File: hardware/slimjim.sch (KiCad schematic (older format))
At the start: 9 parts, among them J1 USB, P1 CONN_01X12, P2 CONN_01X12, P3 CONN_01X12, P4 CONN_01X12, P5 CONN_01X12, P6 CONN_01X12, SW1 SW_PUSH

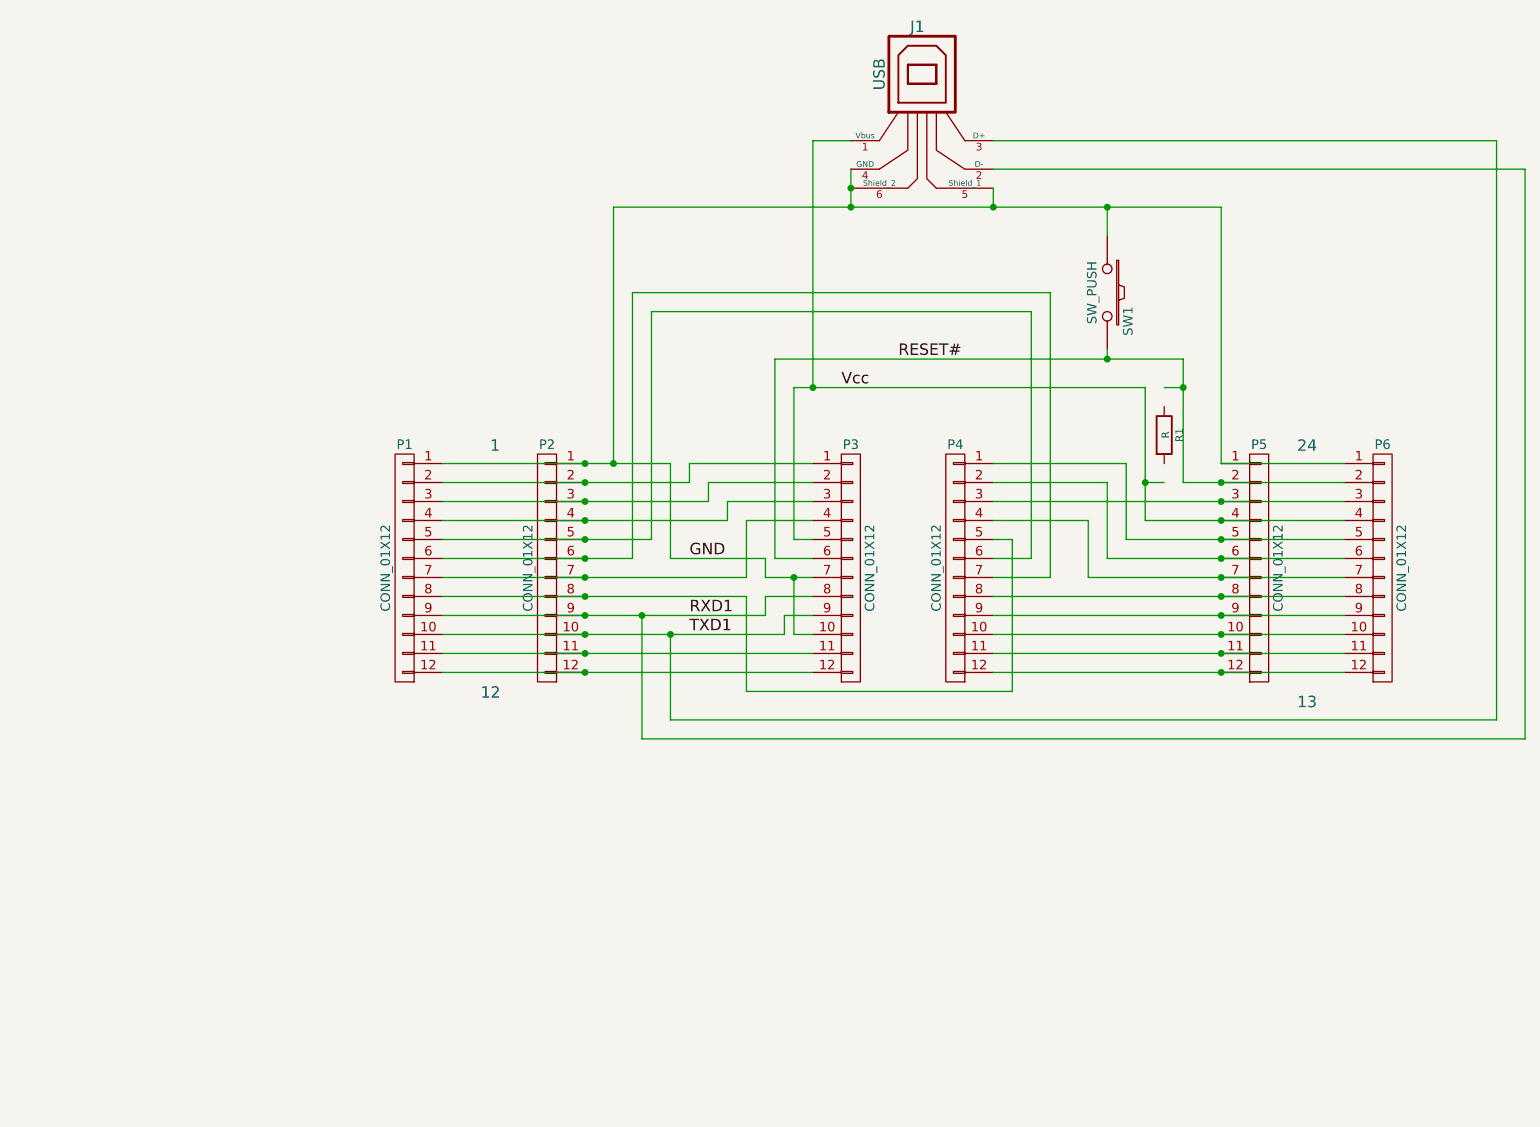
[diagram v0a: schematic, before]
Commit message: Replace generic pin headers with actual parts.
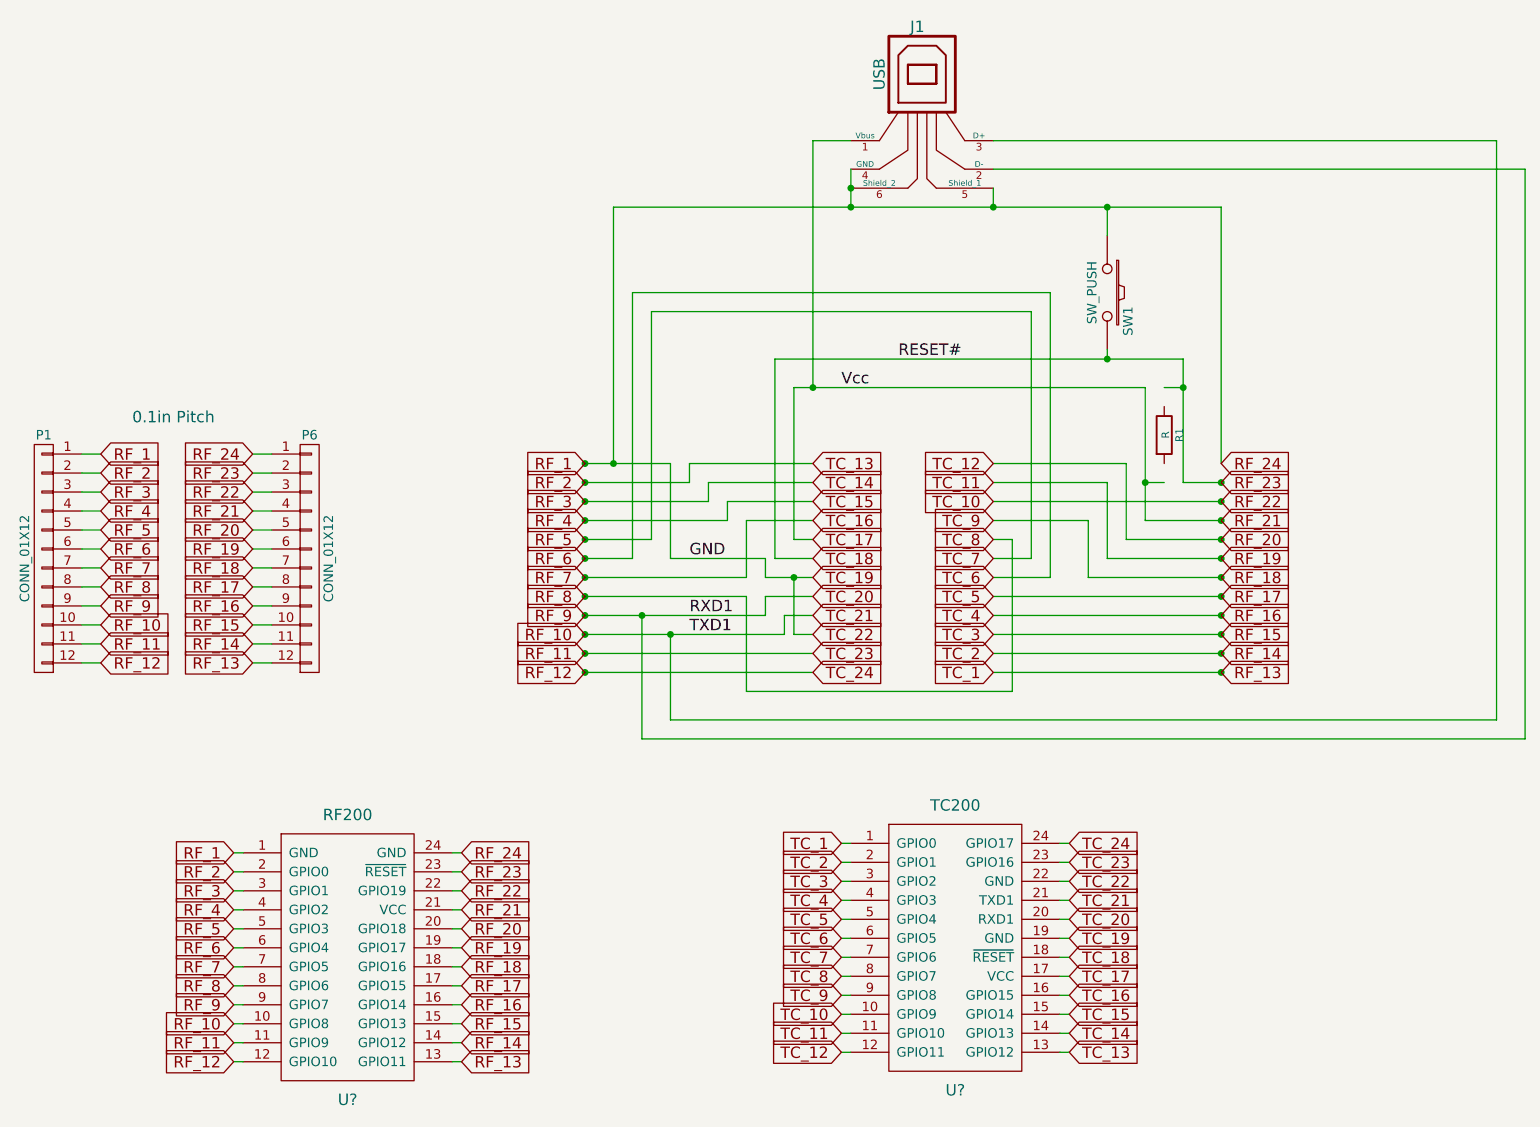
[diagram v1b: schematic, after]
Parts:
- removed P2, P3, P4, P5: CONN_01X12, symbol CONN_01X12
- added U?: RF200, symbol RF200
- added U?: TC200, symbol TC200
- SW1: footprint (none) -> _CrumpPrints:6x6mm_pushbutton
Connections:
- net RF_2: now reaches P1.2 (P2)
- net RF_2: now also U?.13 (GPIO12), U?.2 (GPIO0)
- net RF_11: now reaches P1.11 (P11)
- net RF_11: now also U?.11 (GPIO9), U?.23 (GPIO16)
- net RF_12: now reaches P1.12 (P12)
- net RF_12: now also U?.12 (GPIO10), U?.24 (GPIO17)
- net RF_3: now reaches P1.3 (P3)
- net RF_3: now also U?.14 (GPIO13), U?.3 (GPIO1)
- net RF_4: now reaches P1.4 (P4)
- net RF_4: now also U?.15 (GPIO14), U?.4 (GPIO2)
- net RF_7: now reaches P1.7 (P7)
- net RF_7: now also U?.16 (GPIO15), U?.7 (GPIO5)
- net RF_20: now reaches P6.5 (P5)
- net RF_20: now also U?.12 (GPIO11), U?.20 (GPIO18)
- net RF_15: now reaches P6.10 (P10)
- net RF_15: now also U?.15 (GPIO13), U?.3 (GPIO2)
- net RF_14: now reaches P6.11 (P11)
- net RF_14: now also U?.14 (GPIO12), U?.2 (GPIO1)
- net RF_13: now reaches P6.12 (P12)
- net RF_13: now also U?.1 (GPIO0), U?.13 (GPIO11)
- net RF_19: now reaches P6.6 (P6)
- net RF_19: now also U?.11 (GPIO10), U?.19 (GPIO17)
- net RF_22: now reaches P6.3 (P3)
- net RF_22: now also U?.10 (GPIO9), U?.22 (GPIO19)
- net RF_18: now reaches P6.7 (P7)
- net RF_18: now also U?.18 (GPIO16), U?.9 (GPIO8)
- net RF_8: now reaches P1.8 (P8)
- net RF_8: now also U?.8 (GPIO6), U?.8 (GPIO7)
- net RF_5: now reaches P1.5 (P5)
- net RF_5: now also U?.5 (GPIO3), U?.7 (GPIO6)
- net RF_6: now reaches P1.6 (P6)
- net RF_6: now also U?.6 (GPIO4), U?.6 (GPIO5)
- net RF_17: now reaches P6.8 (P8)
- net RF_17: now also U?.17 (GPIO15), U?.5 (GPIO4)
- net RF_16: now reaches P6.9 (P9)
- net RF_16: now also U?.16 (GPIO14), U?.4 (GPIO3)
- net GND renamed RF_1
- net RF_1: now also U?.1 (GND), U?.19 (GND), U?.22 (GND), U?.24 (GND)
- net RESET# renamed RF_23
- net RF_23: now also U?.18 (~RESET), U?.23 (~RESET)
- net RXD1 renamed RF_9
- net RF_9: now also U?.20 (RXD1), U?.9 (GPIO7)
- net TXD1 renamed RF_10
- net RF_10: now also U?.10 (GPIO8), U?.21 (TXD1)
- net Vcc renamed RF_21
- net RF_21: now also U?.17 (VCC), U?.21 (VCC)
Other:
- note added: "0.1in Pitch"
- note removed: "1"
- note removed: "12"
- note removed: "13"
- note removed: "24"
- moved on the sheet: P1, P6

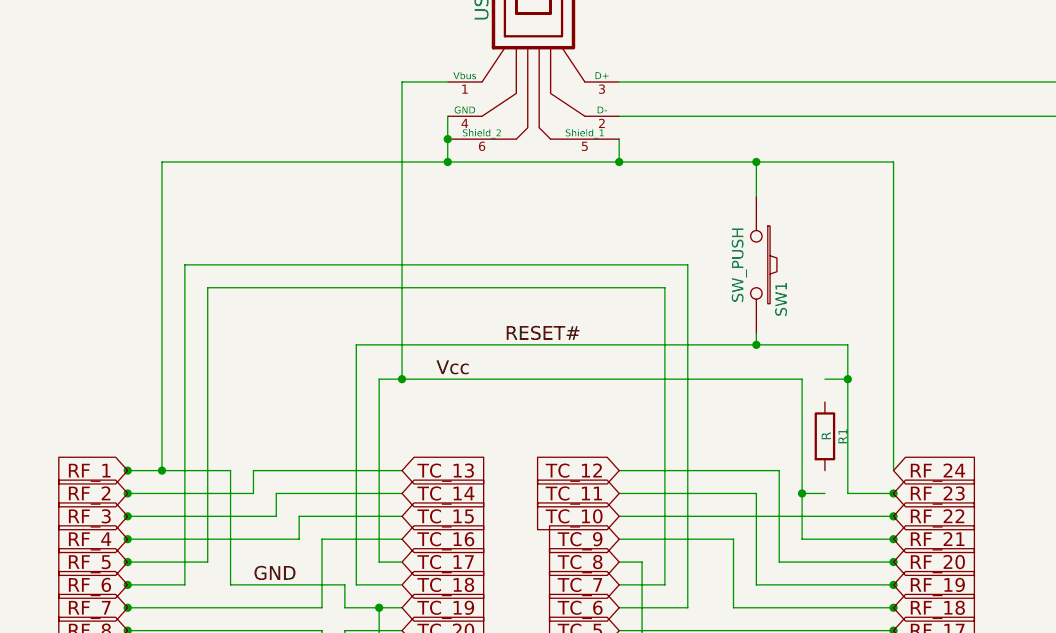
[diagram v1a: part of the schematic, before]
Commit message: Make tiny tweak to a wire in schematic.
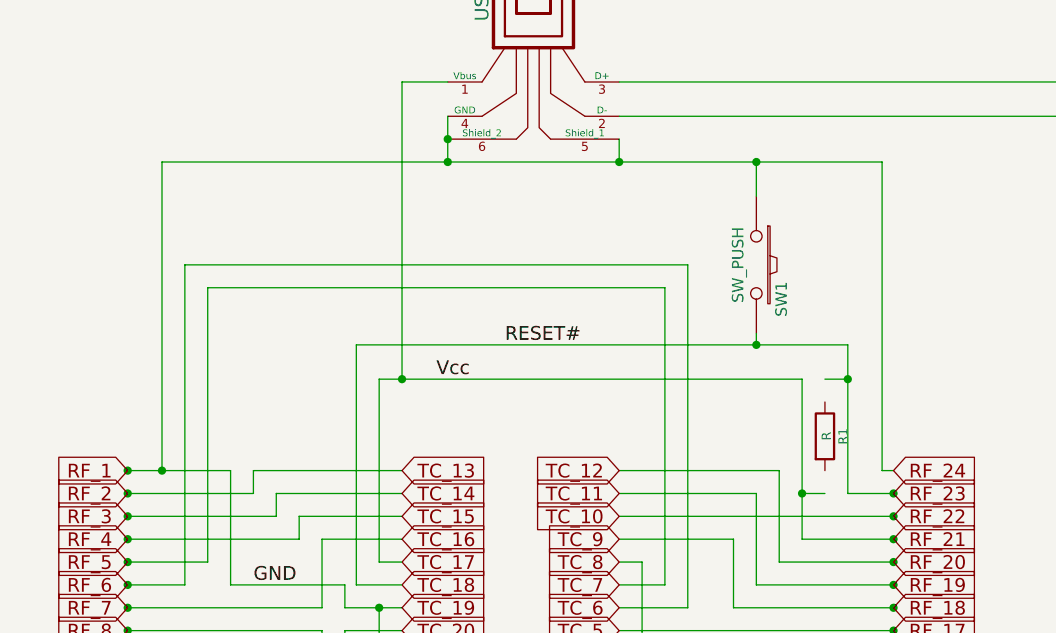
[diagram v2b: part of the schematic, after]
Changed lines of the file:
@@
 	6550 1900 6550 1800
 Wire Wire Line
-	4550 1900 7750 1900
+	4550 1900 7700 1900
 Connection ~ 5800 1800
 Wire Wire Line
@@
 Connection ~ 4400 4350
 Wire Wire Line
-	7750 1900 7750 3250
+	7700 1900 7700 3250
 Connection ~ 6550 1900
 Connection ~ 7750 3350
@@
 Wire Wire Line
 	6950 5250 6900 5250
+Wire Wire Line
+	7700 3250 7750 3250
 $EndSCHEMATC

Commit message: Initial part placement.
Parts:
- J1: footprint (none) -> Connect:USB_A
- P1: footprint (none) -> _CrumpPrints:Header_1x12_100
- P2: renamed from P6; footprint (none) -> _CrumpPrints:Header_1x12_100
- R1: footprint (none) -> Resistors_SMD:R_0805_HandSoldering
- U1: renamed from U?; footprint (none) -> _CrumpPrints:RF200
- U2: renamed from U?; footprint (none) -> _CrumpPrints:TC200
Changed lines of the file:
@@
 F 0 "J1" H 6150 1750 60  0000 C CNN
 F 1 "USB" V 5950 1500 60  0000 C CNN
-F 2 "" H 6200 1350 60  0001 C CNN
+F 2 "Connect:USB_A" H 6200 1350 60  0001 C CNN
 F 3 "" H 6200 1350 60  0000 C CNN
 	1    6200 1350
@@
 Connection ~ 4850 4150
 $Comp
-L CONN_01X12 P6
+L CONN_01X12 P2
 U 1 1 56F37C15
 P 2950 3750
-F 0 "P6" H 2950 4400 50  0000 C CNN
+F 0 "P2" H 2950 4400 50  0000 C CNN
 F 1 "CONN_01X12" V 3050 3750 50  0000 C CNN
-F 2 "" H 2950 3750 60  0001 C CNN
+F 2 "_CrumpPrints:Header_1x12_100" H 2950 3750 60  0001 C CNN
 F 3 "" H 2950 3750 60  0000 C CNN
 	1    2950 3750
@@
 F 0 "P1" H 1550 4400 50  0000 C CNN
 F 1 "CONN_01X12" V 1650 3750 50  0000 C CNN
-F 2 "" H 1550 3750 60  0001 C CNN
+F 2 "_CrumpPrints:Header_1x12_100" H 1550 3750 60  0001 C CNN
 F 3 "" H 1550 3750 60  0000 C CNN
 	1    1550 3750
@@
 F 0 "R1" V 7530 3100 40  0000 C CNN
 F 1 "R" V 7457 3101 40  0000 C CNN
-F 2 "" V 7380 3100 30  0001 C CNN
+F 2 "Resistors_SMD:R_0805_HandSoldering" V 7380 3100 30  0001 C CNN
 F 3 "" H 7450 3100 30  0000 C CNN
 	1    7450 3100
@@
 0.1in Pitch
 $Comp
-L RF200 U?
+L RF200 U1
 U 1 1 56FE09B4
 P 3150 5850
-F 0 "U?" H 3150 5100 60  0000 C CNN
+F 0 "U1" H 3150 5100 60  0000 C CNN
 F 1 "RF200" H 3150 6600 60  0000 C CNN
-F 2 "" H 3100 5850 60  0000 C CNN
+F 2 "_CrumpPrints:RF200" H 3100 5850 60  0001 C CNN
 F 3 "" H 3100 5850 60  0000 C CNN
 	1    3150 5850
@@
 	3750 5300 3700 5300
 $Comp
-L TC200 U?
+L TC200 U2
 U 1 1 56FE1E98
 P 6350 5800
-F 0 "U?" H 6350 5050 60  0000 C CNN
+F 0 "U2" H 6350 5050 60  0000 C CNN
 F 1 "TC200" H 6350 6550 60  0000 C CNN
-F 2 "" H 6300 5800 60  0000 C CNN
+F 2 "_CrumpPrints:TC200" H 6300 5800 60  0001 C CNN
 F 3 "" H 6300 5800 60  0000 C CNN
 	1    6350 5800

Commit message: Refresh project.
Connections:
- net RF_21: now also R1.2
- net RF_23: now also R1.1
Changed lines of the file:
@@
 LIBS:memory
 LIBS:xilinx
-LIBS:special
 LIBS:microcontrollers
 LIBS:dsp
@@
 Wire Wire Line
 	7700 3250 7750 3250
+Wire Wire Line
+	7450 2950 7450 2850
+Wire Wire Line
+	7450 3350 7450 3250
 $EndSCHEMATC

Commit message: Clean up silkscreens for RF200 and TC200.
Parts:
- U1: footprint _CrumpPrints:RF200 -> _CrumpPrints:RF200_nosilk
- U2: footprint _CrumpPrints:TC200 -> _CrumpPrints:TC200_nosilk
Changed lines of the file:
@@
 F 0 "U1" H 3150 5100 60  0000 C CNN
 F 1 "RF200" H 3150 6600 60  0000 C CNN
-F 2 "_CrumpPrints:RF200" H 3100 5850 60  0001 C CNN
+F 2 "_CrumpPrints:RF200_nosilk" H 3100 5850 60  0001 C CNN
 F 3 "" H 3100 5850 60  0000 C CNN
 	1    3150 5850
@@
 F 0 "U2" H 6350 5050 60  0000 C CNN
 F 1 "TC200" H 6350 6550 60  0000 C CNN
-F 2 "_CrumpPrints:TC200" H 6300 5800 60  0001 C CNN
+F 2 "_CrumpPrints:TC200_nosilk" H 6300 5800 60  0001 C CNN
 F 3 "" H 6300 5800 60  0000 C CNN
 	1    6350 5800
